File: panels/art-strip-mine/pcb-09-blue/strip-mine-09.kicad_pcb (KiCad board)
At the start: 2 copper layers, 101.3 x 94.3 mm, 4 parts

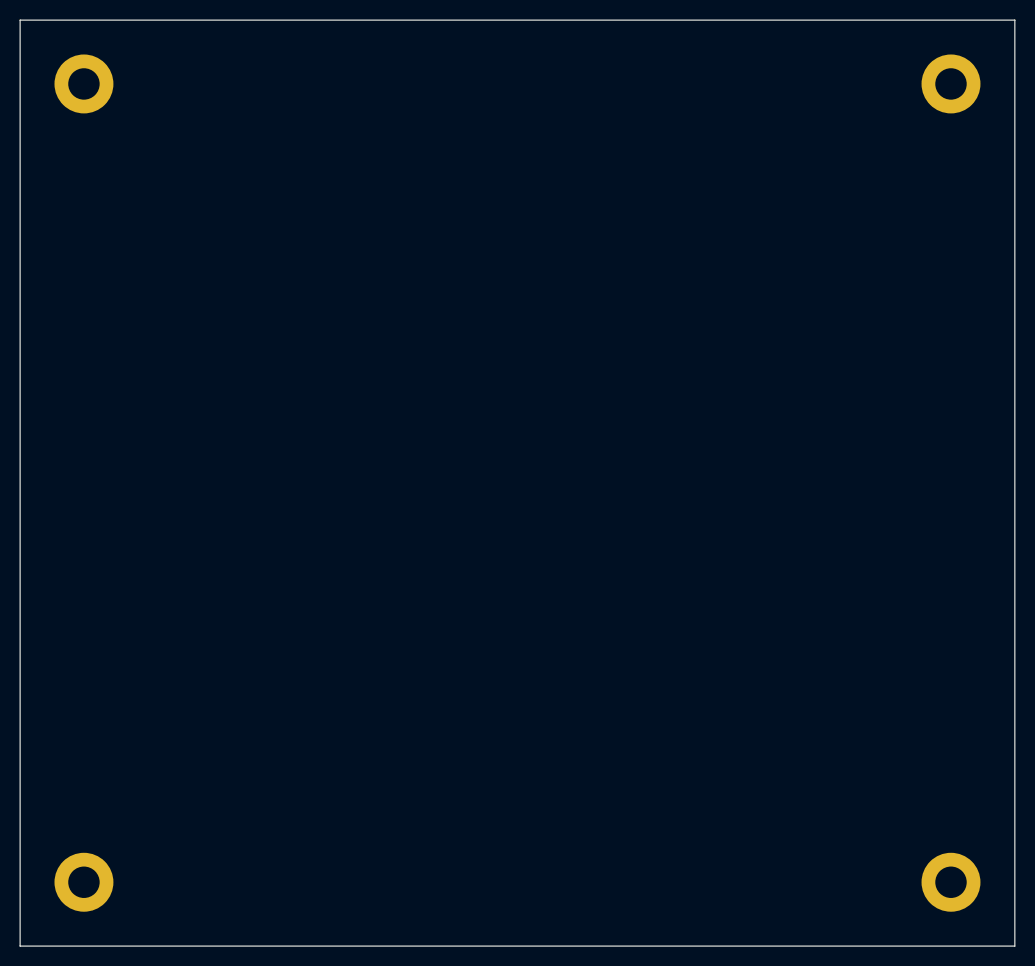
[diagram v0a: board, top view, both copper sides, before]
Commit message: Panelize Strip Mine lower boards and remove blue board copper
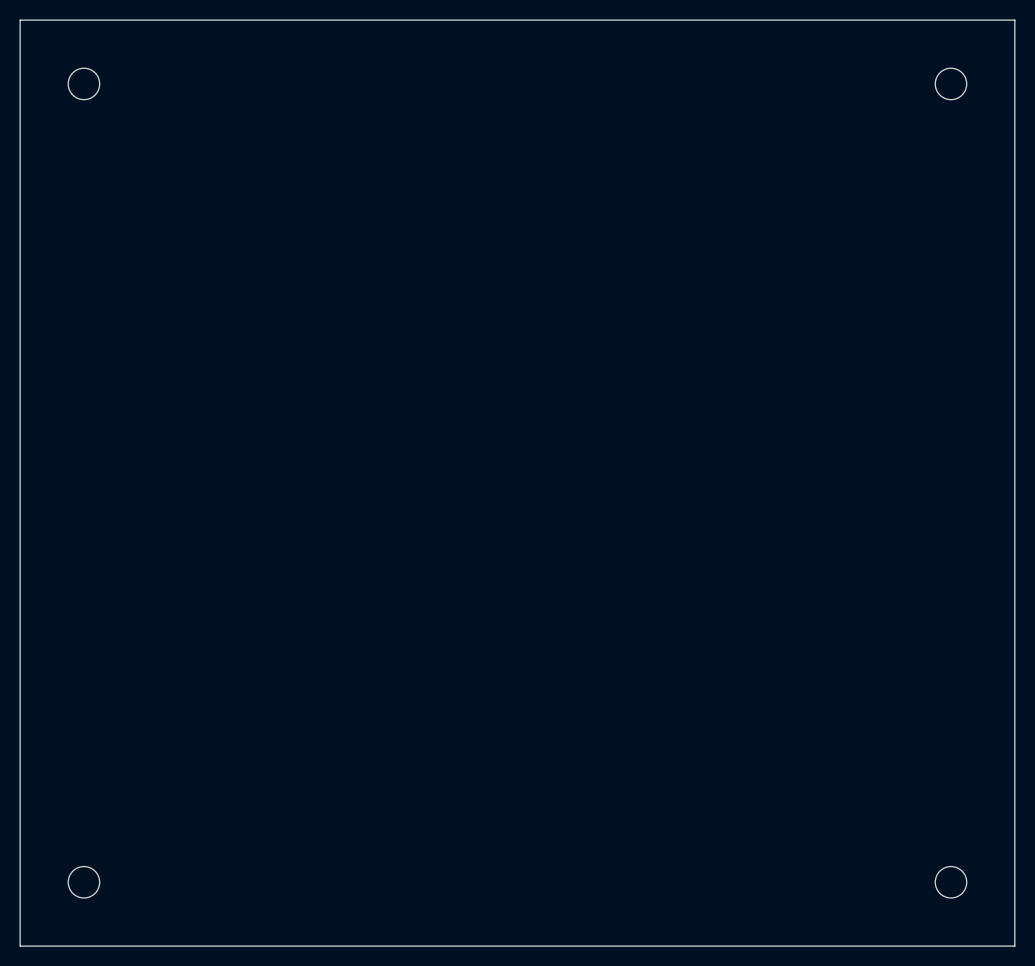
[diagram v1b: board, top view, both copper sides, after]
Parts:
- ? (x4): renamed from REF**; value stack-M3-screw-hole-pad6 -> (none); footprint Takazudo:stack-M3-screw-hole-pad6 -> Takazudo:stack-M3-NPTH
